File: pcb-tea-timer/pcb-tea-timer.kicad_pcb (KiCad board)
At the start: 2 copper layers, 36.1 x 67.1 mm, 10 parts, among them J1 Conn_01x07_Female, J2 Conn_01x02_Female, Q1 2N7002, SW1 SW_Push_Dual, SW2 SW_Push_Dual

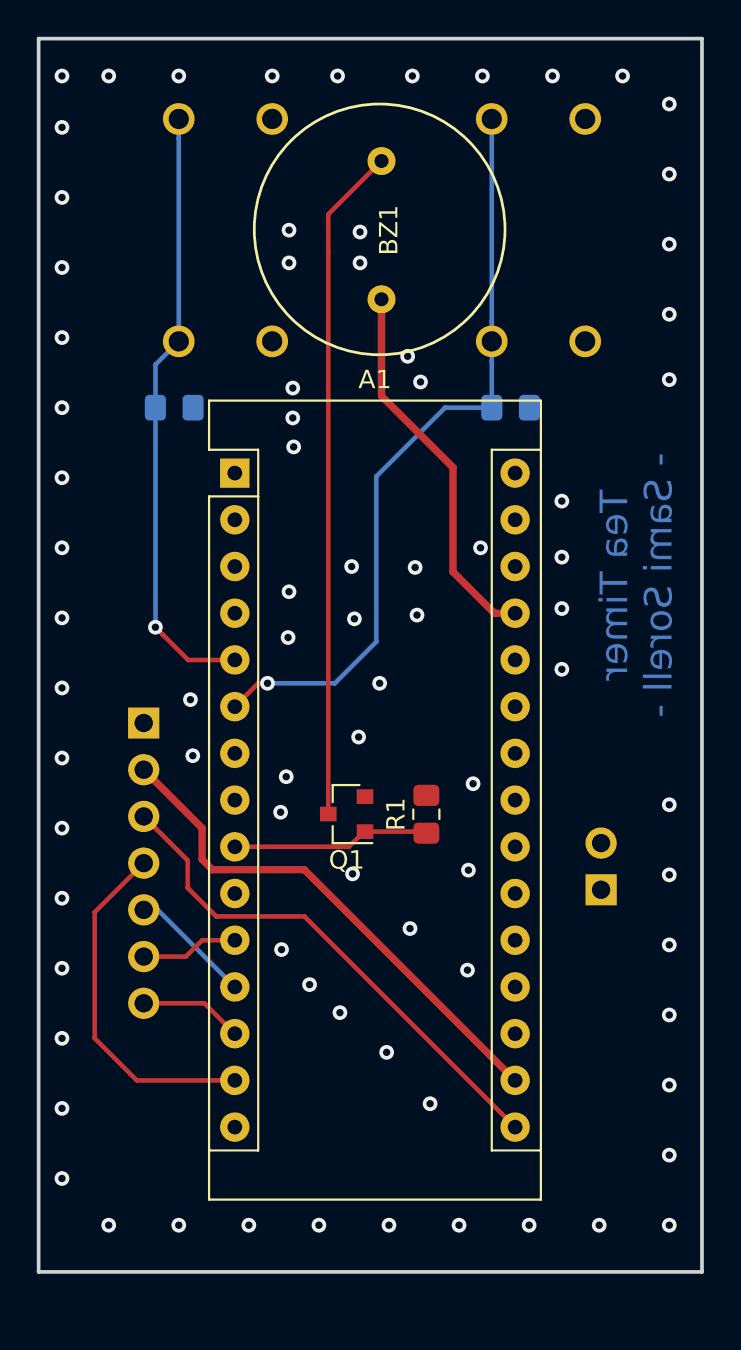
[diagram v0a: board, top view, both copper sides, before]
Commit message: Pcb-tea-timer: fix piezo buzzer driving with a mosfet.
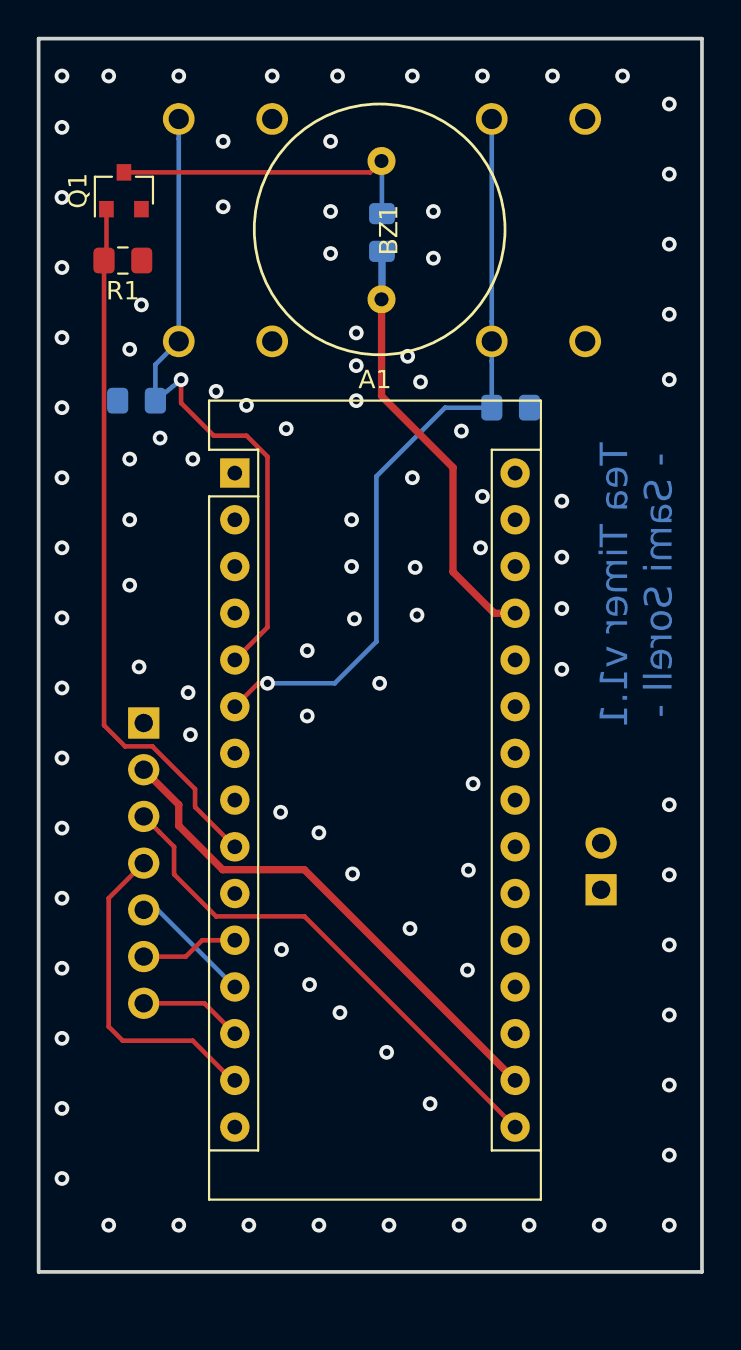
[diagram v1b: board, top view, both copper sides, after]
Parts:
- added R2: 1k, Resistor_SMD:R_0805_2012Metric_Pad1.15x1.40mm_HandSolder, B.Cu at (139.3, 70.5)
- moved Q1 36.0 mm to (125.3, 68.2), turned to 90 degrees
- moved R1 34.3 mm to (125.2, 72.0), turned to 180 degrees
- moved C1 2.09 mm to (126.0, 79.6), turned to 180 degrees
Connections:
- R1 pad 1: Net-(A1-Pad9) -> GND
- R1 pad 2: GND -> Net-(A1-Pad9)
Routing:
- net Net-(A1-Pad9): track 10.8 -> 38.5 mm
- net Net-(BZ1-Pad2): track 36.7 -> 17.1 mm
- net Net-(A1-Pad5): track 33.2 -> 37.1 mm
- net +5V: track 20.8 -> 23.4 mm
- net Net-(A1-Pad14): track 19.2 -> 17.7 mm
- net GND: vias 81 -> 98
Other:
- board text added: "Tea Timer v1.1 - Sami Sorell -"
- board text removed: "Tea Timer - Sami Sorell -"

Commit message: Pcb-tea-timer: add capacitor to support vcc against drops
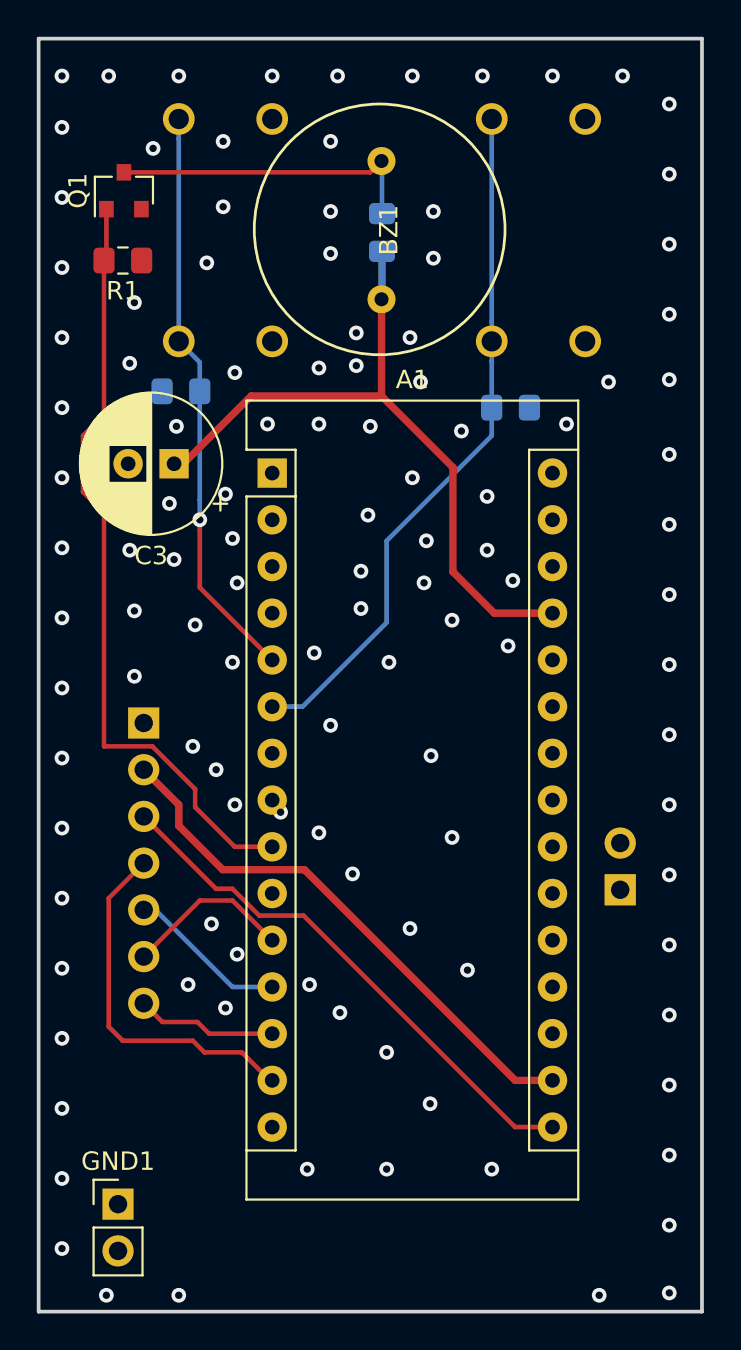
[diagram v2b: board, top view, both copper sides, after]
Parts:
- added C3: 1000uF, Capacitor_THT:CP_Radial_D7.5mm_P2.50mm, F.Cu at (128.0, 83.1)
- added GND1: Conn_01x02_Female, Connector_PinHeader_2.54mm:PinHeader_1x02_P2.54mm_Vertical, F.Cu at (125.0, 123.3)
- moved C1 2.47 mm to (128.4, 79.1)
- moved A1 2.03 mm to (133.3, 83.6)
- moved J2 1.04 mm to (152.3, 106.2)
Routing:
- net +5V: track 23.4 -> 38.2 mm
- net Net-(A1-Pad5): track 37.1 -> 31.5 mm
- net Net-(A1-Pad11): track 5.32 -> 9.14 mm
- net Net-(A1-Pad6): track 41.7 -> 37.9 mm, vias 1 -> 0
- net Net-(A1-Pad9): track 38.5 -> 42.2 mm
- net +3V3: track 27.9 -> 29.9 mm
- net Net-(A1-Pad12): track 6.69 -> 8.72 mm
- net Net-(A1-Pad13): track 5.64 -> 7.67 mm
- net Net-(A1-Pad14): track 17.7 -> 19.8 mm
- net Net-(A1-Pad16): track 28.1 -> 29.2 mm
- net Net-(A1-Pad8): vias 0 -> 1
- net GND: vias 98 -> 115
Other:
- board size 36.1 x 67.1 mm -> 36.1 x 69.2 mm
